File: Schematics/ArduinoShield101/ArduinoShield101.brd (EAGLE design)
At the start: 64 x 53 mm, 18 parts, among them IC1 INA122U

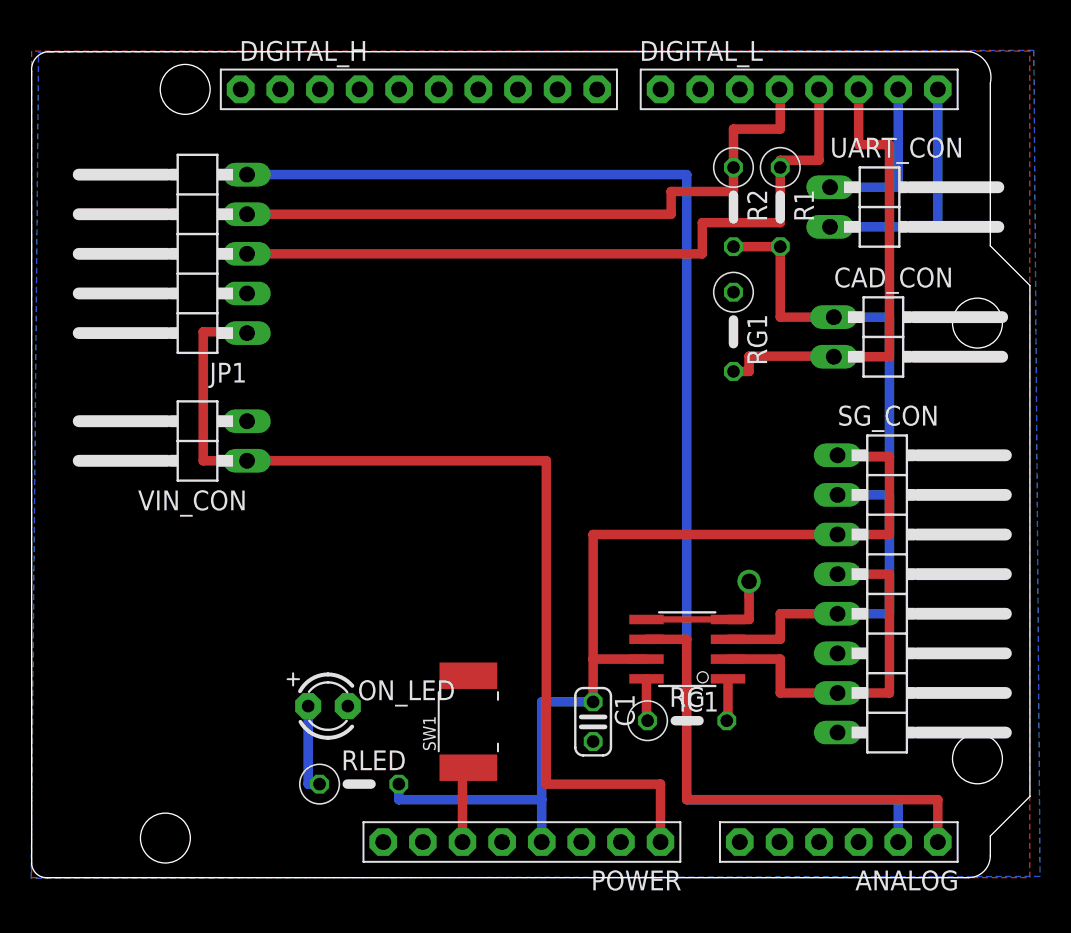
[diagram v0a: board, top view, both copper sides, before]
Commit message: Updated Arduino Shield to the version that was printed.
Includes CAM files.
Some changes must be made to the Shield to ease mounting/soldering.
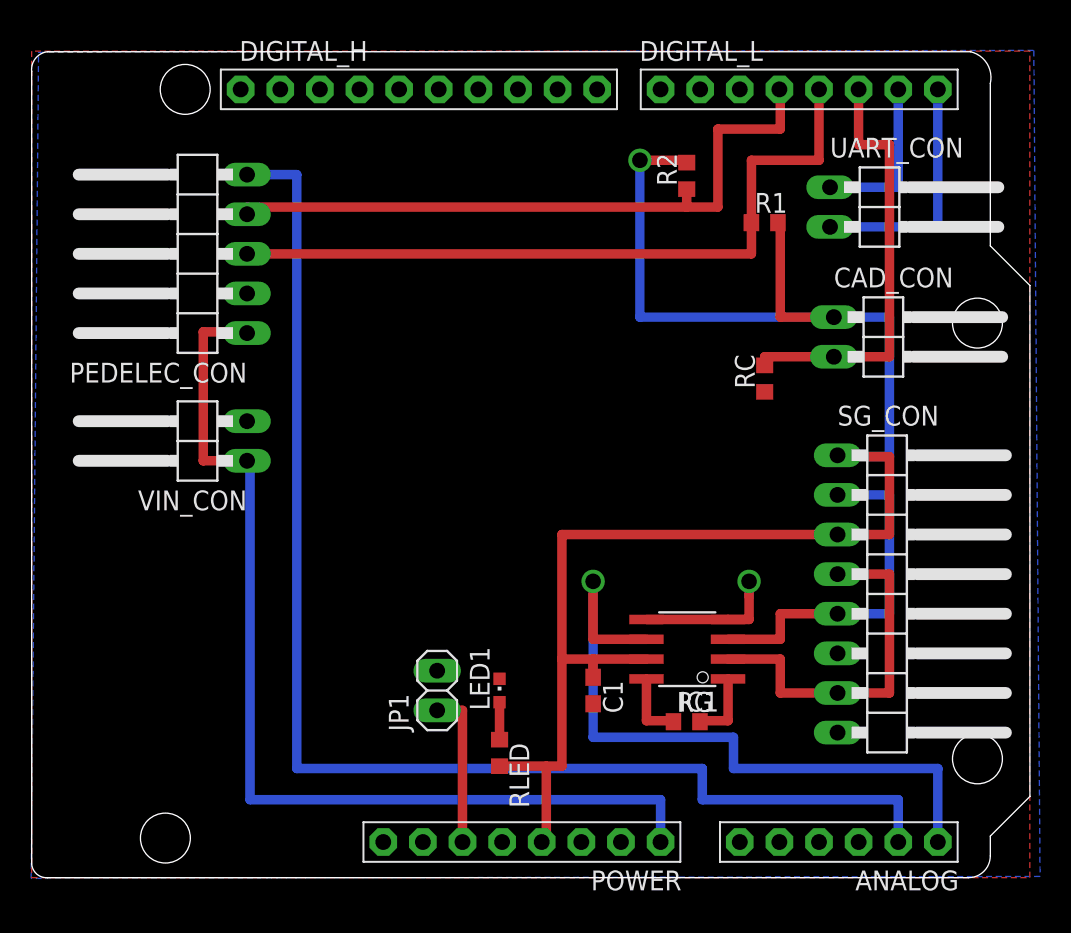
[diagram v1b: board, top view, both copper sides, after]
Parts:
- removed ON_LED: (no value), adafruit:LED3MM
- removed RG1: 10k, rcl:0207/5V
- removed SW1: (no value), adafruit:BTN_CK_KSS
- added LED1: (no value), adafruit:CHIPLED_0603
- added PEDELEC_CON: (no value), pinhead:1X05/90
- added RC: 10k, rcl:R0603
- C1: device rcl:C025-024X044 -> rcl:C0603
- JP1: device pinhead:1X05/90 -> pinhead:1X02
- R1, R2, RG, RLED: device rcl:0207/5V -> rcl:R0603
- moved JP1 32.2 mm to (26.0, 12.0)
- moved RLED 9.22 mm to (30.0, 8.00), turned to 270 degrees
- moved R2 3.61 mm to (42.0, 45.0), turned to 90 degrees
- moved C1 2.00 mm to (36.0, 12.0)
- moved R1 1.41 mm to (47.0, 42.0), turned to 0 degrees
- moved RG 0.07 mm to (42.0, 10.0)
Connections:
- net CAD_IN: now also RC.2; no longer RG1.2
- net GND: now also LED1.C, PEDELEC_CON.2, RC.1; no longer ON_LED.K, RG1.1, SW1.P$2
- net N$4: now also LED1.A; no longer ON_LED.A
- net RESET: now also JP1.1; no longer SW1.P$1
- net SENS_COS: now also PEDELEC_CON.4; no longer JP1.4
- net SENS_SIN: now also PEDELEC_CON.3; no longer JP1.3
- net SENS_TORQ: now also PEDELEC_CON.5; no longer JP1.5
- net V+: now also PEDELEC_CON.1; no longer JP1.1
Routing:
- net +5V: track 90.9 -> 111.2 mm, vias 0 -> 1
- net FORCE_IN: track 31.7 -> 46.0 mm, vias 0 -> 1
- net RESET: track 5.14 -> 10.1 mm
- net N$4: track 5.73 -> 2.40 mm
- net CAD_IN: track 30.1 -> 27.7 mm
- net N$2: track 2.76 -> 4.55 mm
- net N$3: track 2.75 -> 4.48 mm
- net SENS_COS: track 42.3 -> 43.4 mm
